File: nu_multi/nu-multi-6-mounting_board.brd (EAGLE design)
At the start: 70 x 18.2 mm, 7 parts

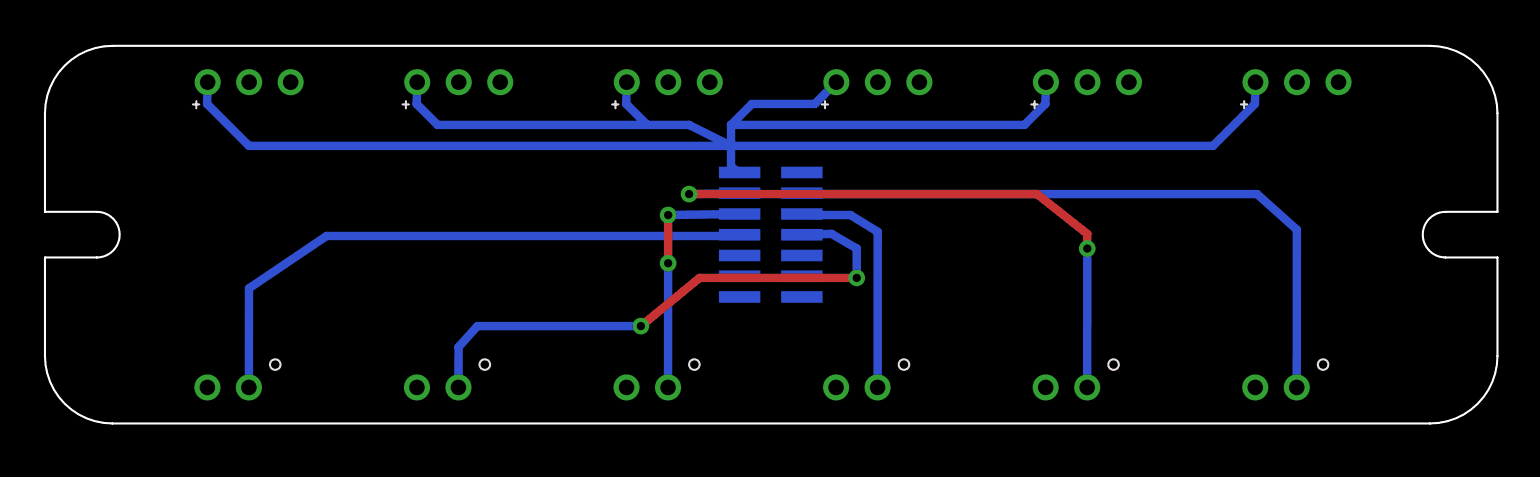
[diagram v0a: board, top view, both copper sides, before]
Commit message: complete board layout
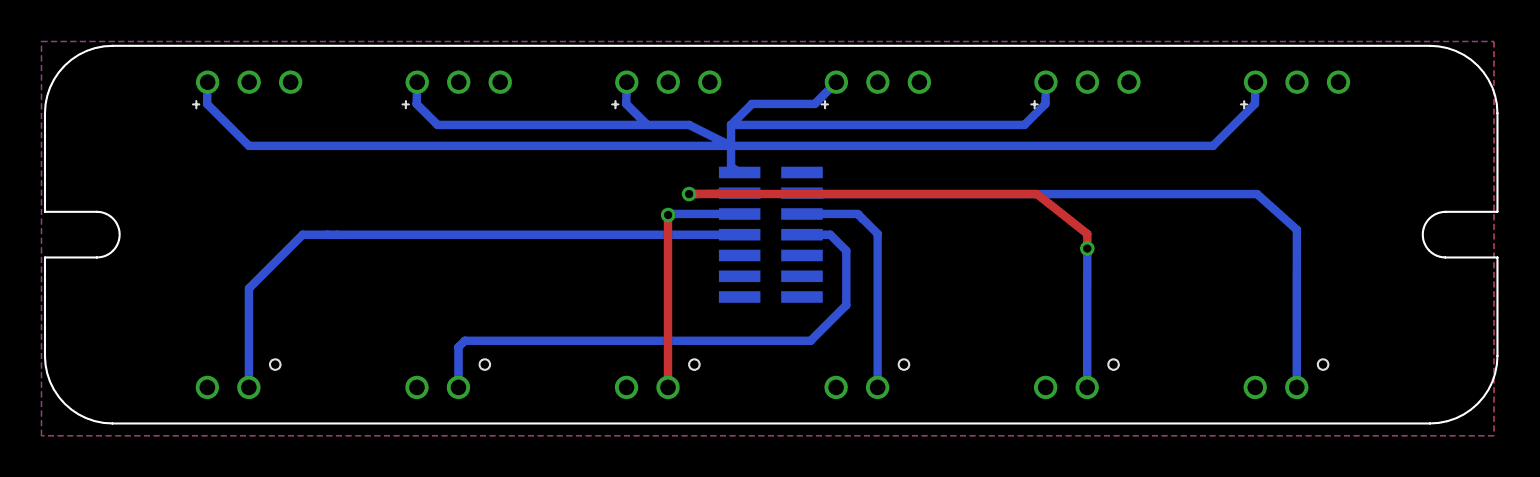
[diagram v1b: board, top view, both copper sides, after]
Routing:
- net CH6: track 28.7 -> 29.5 mm
- net CH3: track 10.8 -> 11.5 mm
- net CH5: track 26.7 -> 26.6 mm, vias 2 -> 0
- net CH4: vias 2 -> 1
- added copper zone on layer 1, net GND
- added copper zone on layer 16, net GND
